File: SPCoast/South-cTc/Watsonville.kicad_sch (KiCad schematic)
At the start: 1 part

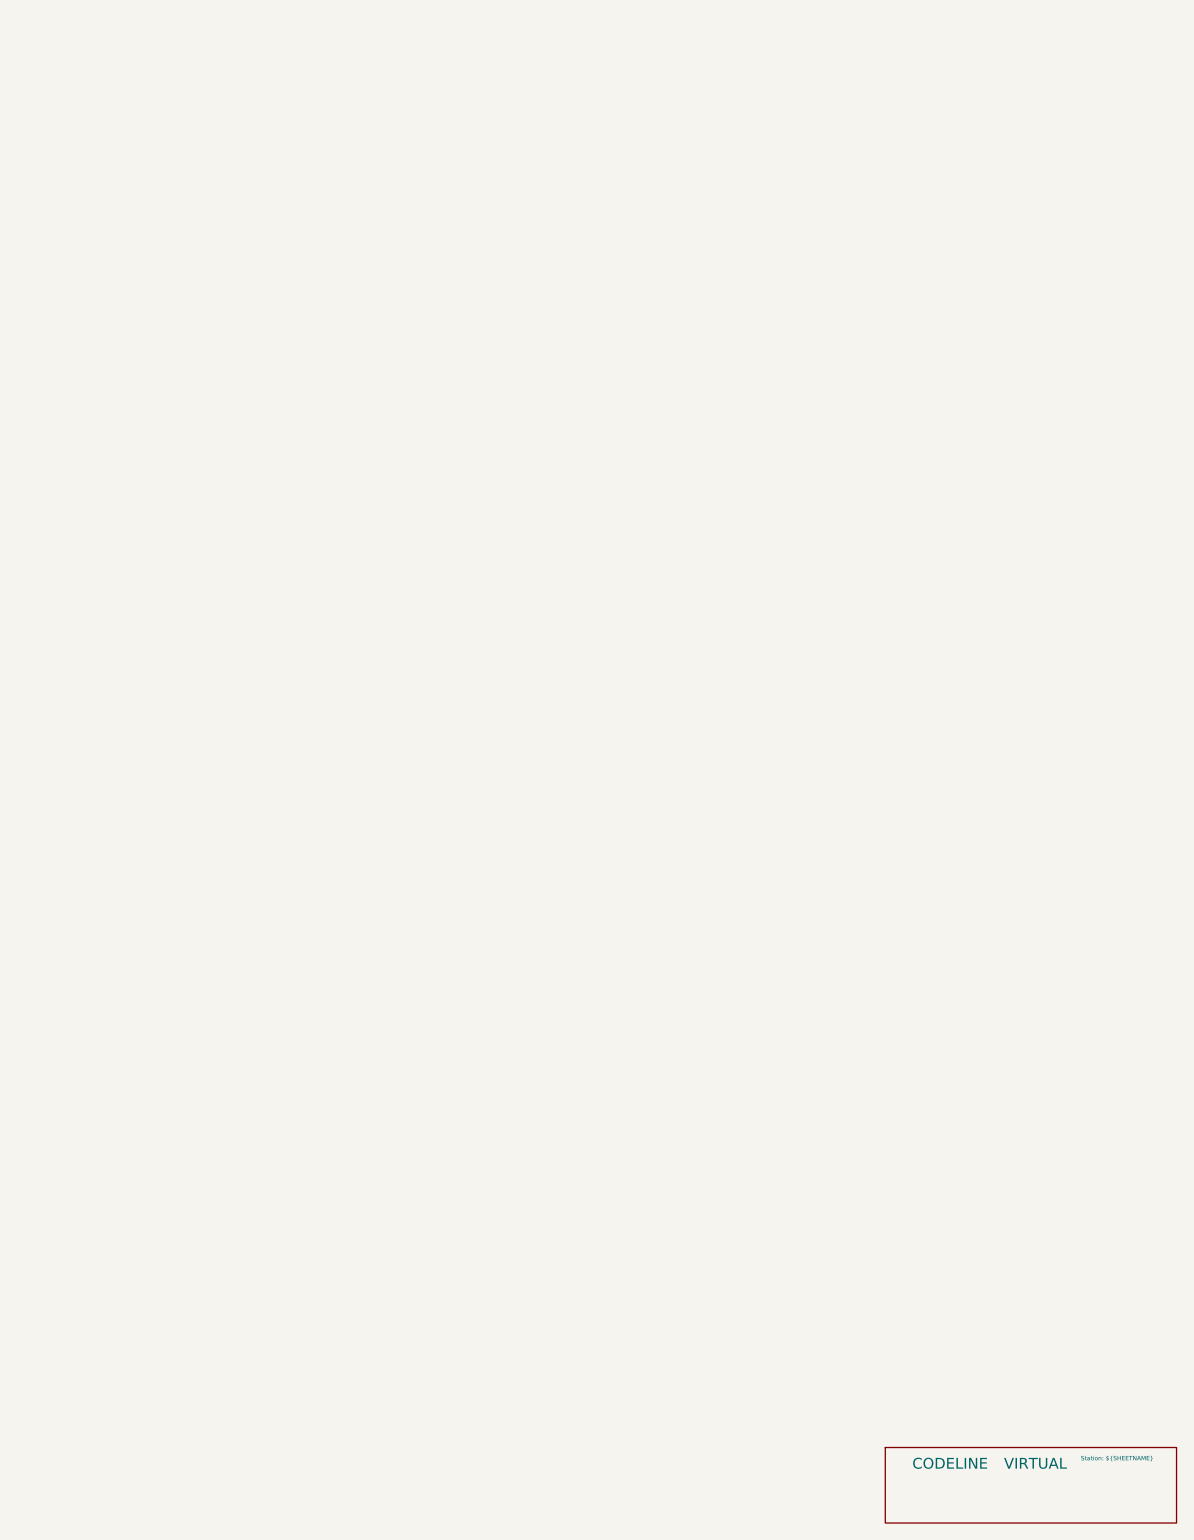
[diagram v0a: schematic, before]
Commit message: SPCoast: derail pin R, track circuit names end in T, code line symbols on the root sheet
Working-tree changes from the 2026-10-01..03 vocabulary review with
FieldUnit-Subdivision (docs/adr/0001-code-line-type-contract.md):

- Switch_Powered_Derail pin 2 is R (through path = REVERSE) in the seven
  plant schematics (library Railroad.kicad_sym renamed alongside; not in git)
- Luchessa track circuits renamed to end in T (1SAT, 2NAAT, ...); MC1 moved
  to CP Gilroy's house
- South-cTc: transports (MQTT, TimeCode, CMRInet, Loconet) on the root
  sheet on the CtcMachine Transports pin; field stations as encoding
  instances on the Luchessa sheet; two Luchessa lamp tokens renamed
- Six plant projects (Christopher, Corporal, GilroyCalTrain,
  GilroyInterchange, Sargent, Watsonville) added as drawn so far; Watsonville
  updated 2026-10-02

Co-Authored-By: Claude Fable 5.1 <noreply@anthropic.com>
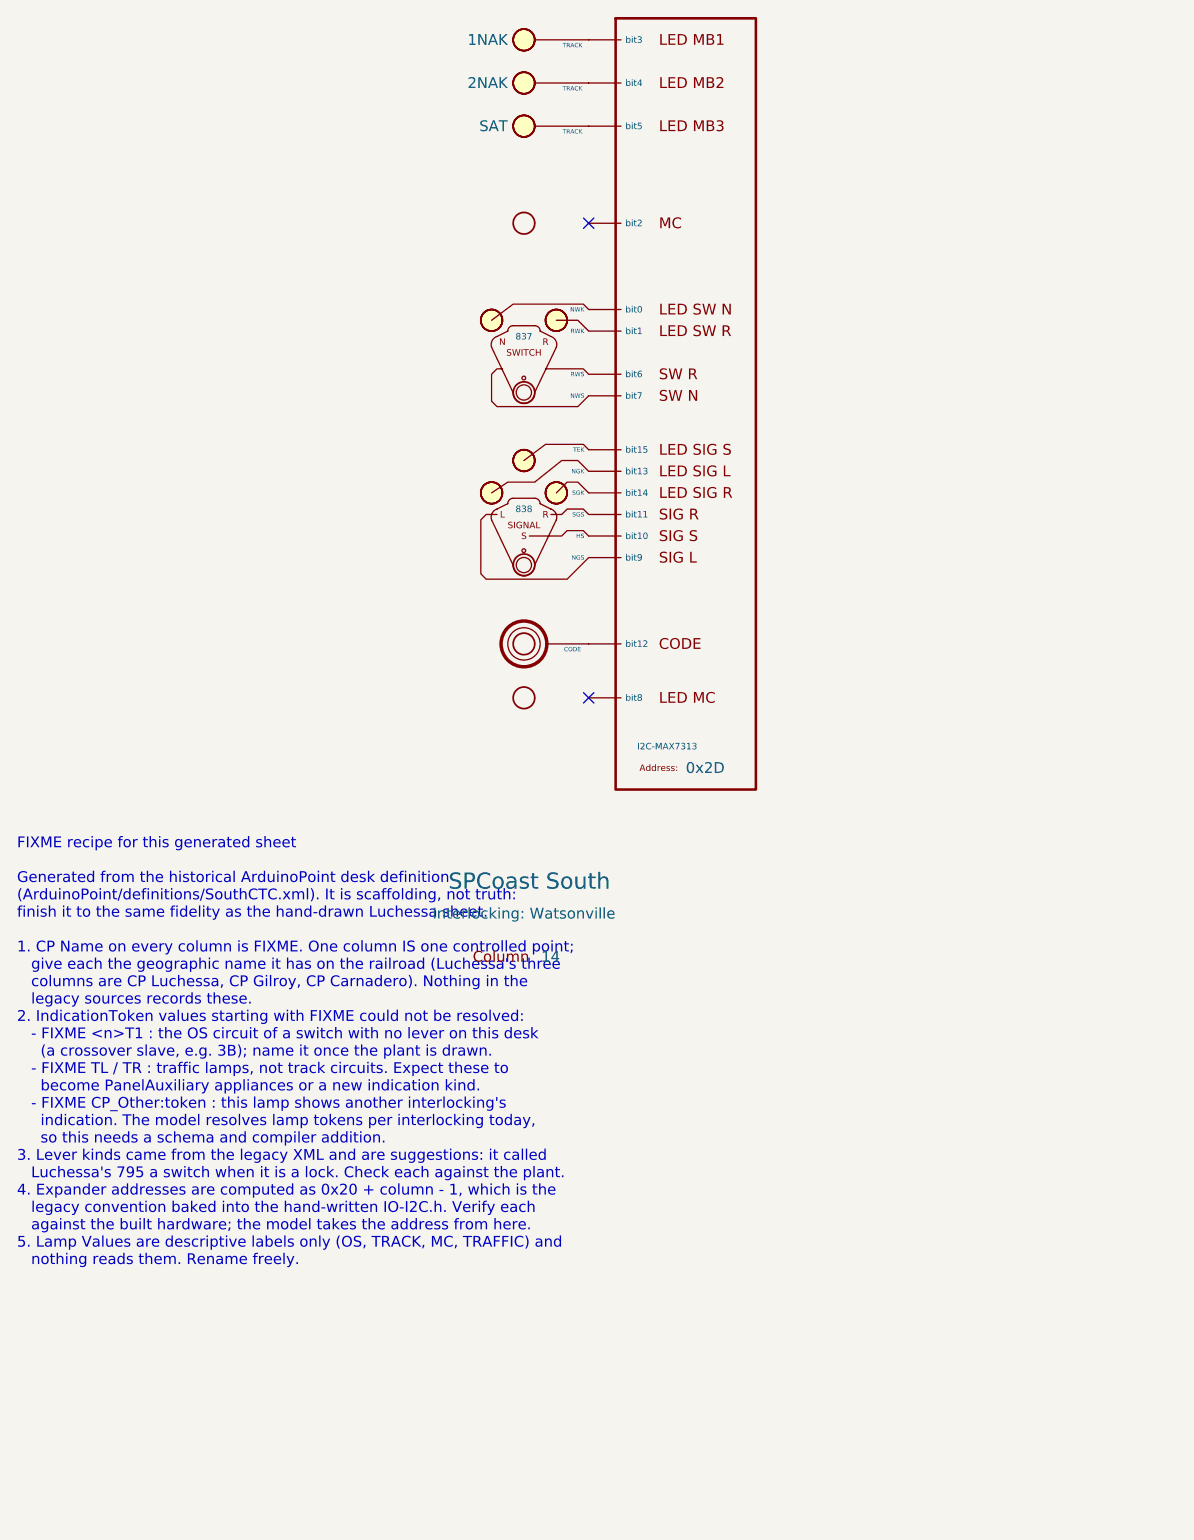
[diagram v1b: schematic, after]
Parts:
- removed CODELINE7: VIRTUAL, symbol RailroadPanel:Codeline-Virtual
- added CDE14: CODE, symbol RailroadPanel:PanelCode
- added COL34: 14, symbol RailroadPanel:PanelColumn
- added LMP141, LMP142, LMP143: TRACK, symbol RailroadPanel:PanelLamp-YELLOW
- added SGL14: 838, symbol RailroadPanel:PanelSignal
- added SWL14: 837, symbol RailroadPanel:PanelSwitch
- added U34: 0x2D, symbol RailroadPanel:PanelColumn-MAX7313
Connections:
- new net: COL34.6 (Column), SGL14.1 (Column)
- new net: SGL14.2 (NGS), U34.10 (bit9)
- new net: SGL14.3 (HS), U34.11 (bit10)
- new net: SGL14.4 (SGS), U34.12 (bit11)
- new net: SGL14.5 (SGK), U34.15 (bit14)
- new net: SGL14.6 (NGK), U34.14 (bit13)
- new net: SGL14.7 (TEK), U34.16 (bit15)
- new net: COL34.1 (Column), LMP141.1 (Column)
- new net: LMP141.2 (LAMP), U34.4 (bit3)
- new net: COL34.3 (Column), LMP143.1 (Column)
- new net: LMP143.2 (LAMP), U34.6 (bit5)
- new net: SWL14.5 (NWK), U34.1 (bit0)
- new net: CDE14.2 (CODE), U34.13 (bit12)
- new net: SWL14.4 (RWK), U34.2 (bit1)
- new net: LMP142.2 (LAMP), U34.5 (bit4)
- new net: SWL14.3 (RWS), U34.7 (bit6)
- new net: SWL14.2 (NWS), U34.8 (bit7)
- new net: CDE14.1 (Column), COL34.7 (Column)
- new net: COL34.5 (Column), SWL14.1 (Column)
- new net: COL34.2 (Column), LMP142.1 (Column)
- no-connect marks 0 -> 2
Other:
- note added: "FIXME recipe for this generated sheet Generated from the historical ArduinoPoint desk definition (ArduinoPoint/definitions/SouthCTC.xml). It is scaffolding, not truth: finish it to the same fidelity as the hand-drawn Luchessa sheet. 1. CP Name on every column is FIXME. One column IS one controlled point; give each the geographic name it has on the railroad (Luchessa's three columns are CP Luchess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"

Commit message: SPCoast: Address field and Kind on PanelColumn-MAX7313; encoding Values; HBA; Watsonville update
Owner's drawing changes of 2026-10-02..03 (FieldUnit-Subdivision ADR 0002 D18
and the owner's responses):

- PanelColumn-MAX7313: the expander address moves from the Value to an
  Address field (Value is ${Address}); BusKind renamed Kind (I2C-MAX7313)
- Luchessa encoding symbols: Value "US&S 506 time-coded DC pulses"
- Sargent: HBD renamed HBA; traffic indications [NSEW]FLK
- Watsonville schematic brought to a usable state
- Luchessa plant: track circuits end in T; MC1 at CP Gilroy's house

Co-Authored-By: Claude Fable 5.1 <noreply@anthropic.com>
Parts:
- U34: Address (none) -> 0x2D; BusKind I2C-MAX7313 -> (none); Kind (none) -> I2C-MAX7313
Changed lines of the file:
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@@
 		(property "Value" "0x2D"
 			(at 99.06 112.395 0)
+			(hide yes)
 			(show_name no)
 			(do_not_autoplace yes)
@@
 			)
 		)
-		(property "BusKind" "I2C-MAX7313"
+		(property "Role" "IODRIVER"
+			(at 97.79 107.315 0)
+			(hide yes)
+			(show_name no)
+			(do_not_autoplace no)
+			(effects
+				(font
+					(size 1.27 1.27)
+				)
+			)
+		)
+		(property "Kind" "I2C-MAX7313"
 			(at 93.345 109.855 0)
 			(show_name no)
-			(do_not_autoplace yes)
+			(do_not_autoplace no)
 			(effects
 				(font
@@
 			)
 		)
-		(property "Role" "IODRIVER"
-			(at 99.06 72.39 0)
-			(hide yes)
+		(property "Address" "0x2D"
+			(at 101.854 112.522 0)
 			(show_name no)
 			(do_not_autoplace no)

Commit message: SPCoast: owner's edits: NextCP names, Christopher heads and masts, Sargent milepost, Watsonville circuits and desk tokens (baseline)
- NextCP values name interlockings: GilroyCalTrain CP2 -> Gilroy Interchange;
  Luchessa CP1 -> Gilroy Interchange, CP2 -> Hollister, CP3 and CP4 ->
  Christopher.
- Christopher: the two unnamed dwarf masts, their IRJ-Signals (now plain IRJs)
  and heads removed; remaining heads lettered A, B, C.
- Sargent MAIN HOUSE Milepost 83.5.
- Watsonville circuits SDT -> 0DT and SAT -> 0AT; desk tokens 0DT, 0AT, AT and
  Watsonville:837T1 follow.

Verified: netlists rebuild (Christopher 30, Corporal 27, GilroyCalTrain 28,
GilroyInterchange 23, Luchessa 35, Sargent 19, Watsonville 97, South-cTc 341);
Christopher has no mast or head diagnostics left; desk compiles to 75
appliances, 137 bindings, 14 columns; no root-UUID regression.

Co-Authored-By: Claude Sonnet 5.5 <noreply@anthropic.com>
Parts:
- LMP141: IndicationToken 1NAK -> 0DT
- LMP142: IndicationToken 2NAK -> 0AT
- LMP143: IndicationToken SAT -> AT
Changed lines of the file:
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@@
 			)
 		)
-		(property "IndicationToken" "1NAK"
+		(property "IndicationToken" "0DT"
 			(at 78.105 26.67 0)
 			(show_name no)
@@
 			)
 		)
-		(property "IndicationToken" "SAT"
+		(property "IndicationToken" "AT"
 			(at 78.105 36.83 0)
 			(show_name no)
@@
 			)
 		)
-		(property "IndicationToken" "2NAK"
+		(property "IndicationToken" "0AT"
 			(at 78.105 31.75 0)
 			(show_name no)

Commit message: SPCoast: owner's edits: Watsonville virtual indications 0100T and 0101T, circuits 01T..03T, desk tokens (baseline)
Includes typos in the member lists (a period for a comma, a missing 25T1, a stray 03T), corrected in the next commit.

Co-Authored-By: Claude Sonnet 5.5 <noreply@anthropic.com>
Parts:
- LMP141: IndicationToken 0DT -> 0101T
- LMP142: IndicationToken 0AT -> 0100T
- LMP143: IndicationToken AT -> 01T
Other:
- note removed: "FIXME recipe for this generated sheet Generated from the historical ArduinoPoint desk definition (ArduinoPoint/definitions/SouthCTC.xml). It is scaffolding, not truth: finish it to the same fidelity as the hand-drawn Luchessa sheet. 1. CP Name on every column is FIXME. One column IS one controlled point; give each the geographic name it has on the railroad (Luchessa's three columns are CP Luchess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"
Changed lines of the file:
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@@
 		(comment 1 "JPlocher")
-	)
-	(text "FIXME recipe for this generated sheet\n\nGenerated from the historical ArduinoPoint desk definition\n(ArduinoPoint/definitions/SouthCTC.xml). It is scaffolding, not truth:\nfinish it to the same fidelity as the hand-drawn Luchessa sheet.\n\n1. CP Name on every column is FIXME. One column IS one controlled point;\n   give each the geographic name it has on the railroad (Luchessa's three\n   columns are CP Luchessa, CP Gilroy, CP Carnadero). Nothing in the\n   legacy sources records these.\n2. IndicationToken values starting with FIXME could not be resolved:\n   - FIXME <n>T1 : the OS circuit of a switch with no lever on this desk\n     (a crossover slave, e.g. 3B); name it once the plant is drawn.\n   - FIXME TL / TR : traffic lamps, not track circuits. Expect these to\n     become PanelAuxiliary appliances or a new indication kind.\n   - FIXME CP_Other:token : this lamp shows another interlocking's\n     indication. The model resolves lamp tokens per interlocking today,\n     so this needs a schema and compiler addition.\n3. Lever kinds came from the legacy XML and are suggestions: it called\n   Luchessa's 795 a switch when it is a lock. Check each against the plant.\n4. Expander addresses are computed as 0x20 + column - 1, which is the\n   legacy convention baked into the hand-written IO-I2C.h. Verify each\n   against the built hardware; the model takes the address from here.\n5. Lamp Values are descriptive labels only (OS, TRACK, MC, TRAFFIC) and\n   nothing reads them. Rename freely.\n"
-		(exclude_from_sim no)
-		(at 20.32 120.65 0)
-		(effects
-			(font
-				(size 1.27 1.27)
-			)
-			(justify left top)
-		)
 	)
 	(no_connect
@@
 			)
 		)
-		(property "IndicationToken" "0DT"
+		(property "IndicationToken" "0101T"
 			(at 78.105 26.67 0)
 			(show_name no)
@@
 			)
 		)
-		(property "IndicationToken" "AT"
+		(property "IndicationToken" "01T"
 			(at 78.105 36.83 0)
 			(show_name no)
@@
 			)
 		)
-		(property "IndicationToken" "0AT"
+		(property "IndicationToken" "0100T"
 			(at 78.105 31.75 0)
 			(show_name no)

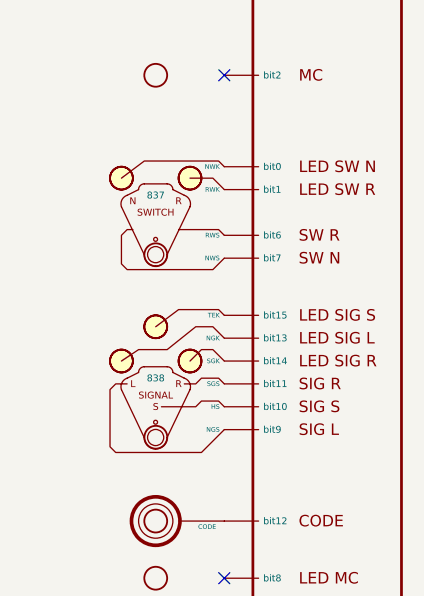
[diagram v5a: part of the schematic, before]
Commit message: chore(kicad): refresh instances to the ADR 0003 libraries (InterlockingPlant 95f53e2)
- Desk sheets (South-cTc/*) and the Sargent sandbox: embedded PanelSwitch, PanelLock,
  PanelSignal, PanelMCall, PanelCode, PanelLamp-*, PanelColumn-MAX7313 definitions refreshed
  from the library (refresh_embedded.py, checked against the pre-pass library: only Description
  text had drifted). Instance Role APPLIANCE -> PANEL (77).
- Plant sheets: powered-switch instance Kind SWITCH_POWERED -> SWITCH_REMOTE (21), matching the
  library (sweep_role_kind_fields.py).

Verified:
- verify_symbol_diff.py: same symbols, lib_ids and positions; only Role/Kind changed.
- Nets unchanged: Christopher 30, Corporal 27, GilroyCalTrain 28, GilroyInterchange 23,
  Luchessa 35, Sargent 61, Watsonville 99, South-cTc 341.
- parse_kicad_plant.py --format text identical before/after for all seven plants.
- Desk compile 75/137/14, diagnostics identical; the 7 desk locks bind WLS/~{WLS}/~{WLK}/WLK
  to the bits that were NWS/RWS/RWK/NWK.
- No sheet or project outside Luchessa carries the copied root UUID.

Co-Authored-By: Claude Opus 5.5 <noreply@anthropic.com>
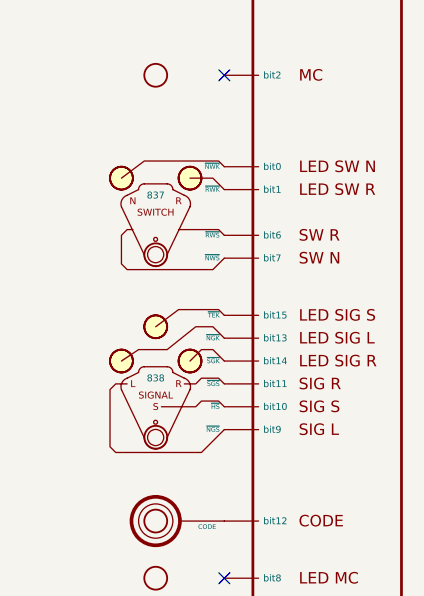
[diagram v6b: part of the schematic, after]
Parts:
- CDE14, LMP141, LMP142, LMP143, SGL14, SWL14: Role APPLIANCE -> PANEL
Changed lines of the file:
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@@
 			)
 		)
-		(property "Role" "APPLIANCE"
+		(property "Role" "PANEL"
 			(at 80.01 92.71 0)
 			(hide yes)
@@
 			)
 		)
-		(property "Role" "APPLIANCE"
+		(property "Role" "PANEL"
 			(at 80.01 24.13 0)
 			(hide yes)
@@
 			)
 		)
-		(property "Role" "APPLIANCE"
+		(property "Role" "PANEL"
 			(at 80.01 34.29 0)
 			(hide yes)
@@
 			)
 		)
-		(property "Role" "APPLIANCE"
+		(property "Role" "PANEL"
 			(at 80.01 90.17 0)
 			(hide yes)
@@
 			)
 		)
-		(property "Role" "APPLIANCE"
+		(property "Role" "PANEL"
 			(at 80.645 76.2 0)
 			(hide yes)
@@
 			)
 		)
-		(property "Role" "APPLIANCE"
+		(property "Role" "PANEL"
 			(at 80.01 29.21 0)
 			(hide yes)

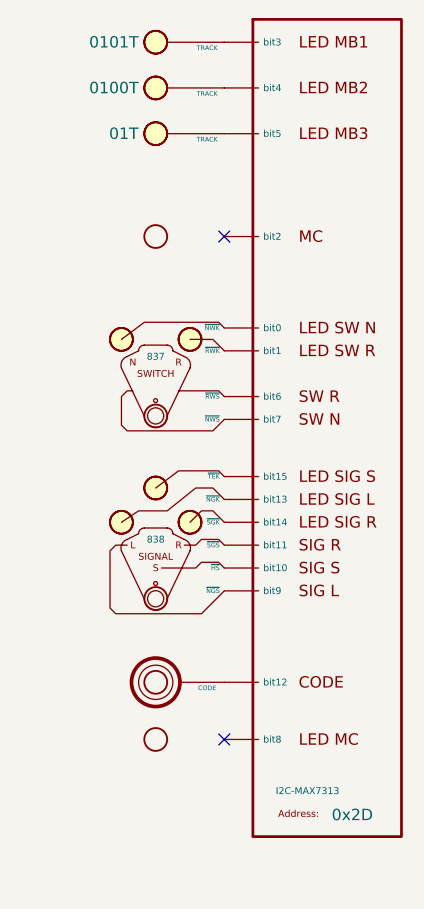
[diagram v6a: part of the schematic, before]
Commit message: chore(kicad): desk sheets to Driver-I2C-MAX7313 and the PanelLock Kind (InterlockingPlant owner review)
- 14 desk expanders: lib_id RailroadPanel:PanelColumn-MAX7313 -> Driver-I2C-MAX7313, embedded
  definition refreshed (pins A1..B8, same numbers and positions).
- 8 PanelLock instances: Kind LOCK_LEVER -> LOCK_LEVER_2LAMP_2CONTACT (7 desk, 1 Sargent sandbox).

Verified:
- verify_symbol_diff.py: only those lib_id and Kind changes.
- South-cTc 341 nets, Sargent 61; desk compile 75/137/14 with bindings identical to e2c1093.

Co-Authored-By: Claude Opus 5.5 <noreply@anthropic.com>
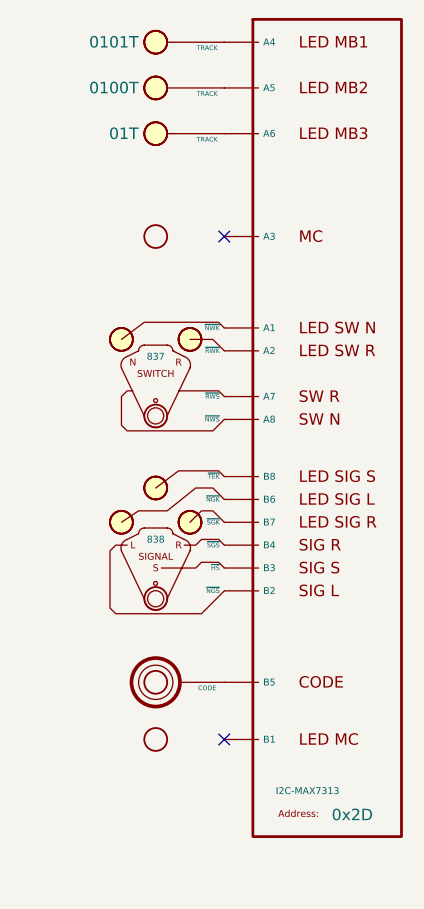
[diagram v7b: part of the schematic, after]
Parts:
- U34: symbol RailroadPanel:PanelColumn-MAX7313 -> RailroadPanel:Driver-I2C-MAX7313
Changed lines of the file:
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@@
 	)
 	(symbol
-		(lib_id "RailroadPanel:PanelColumn-MAX7313")
+		(lib_id "RailroadPanel:Driver-I2C-MAX7313")
 		(at 99.06 72.39 0)
 		(unit 1)
